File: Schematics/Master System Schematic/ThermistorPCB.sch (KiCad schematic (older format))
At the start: 0 parts

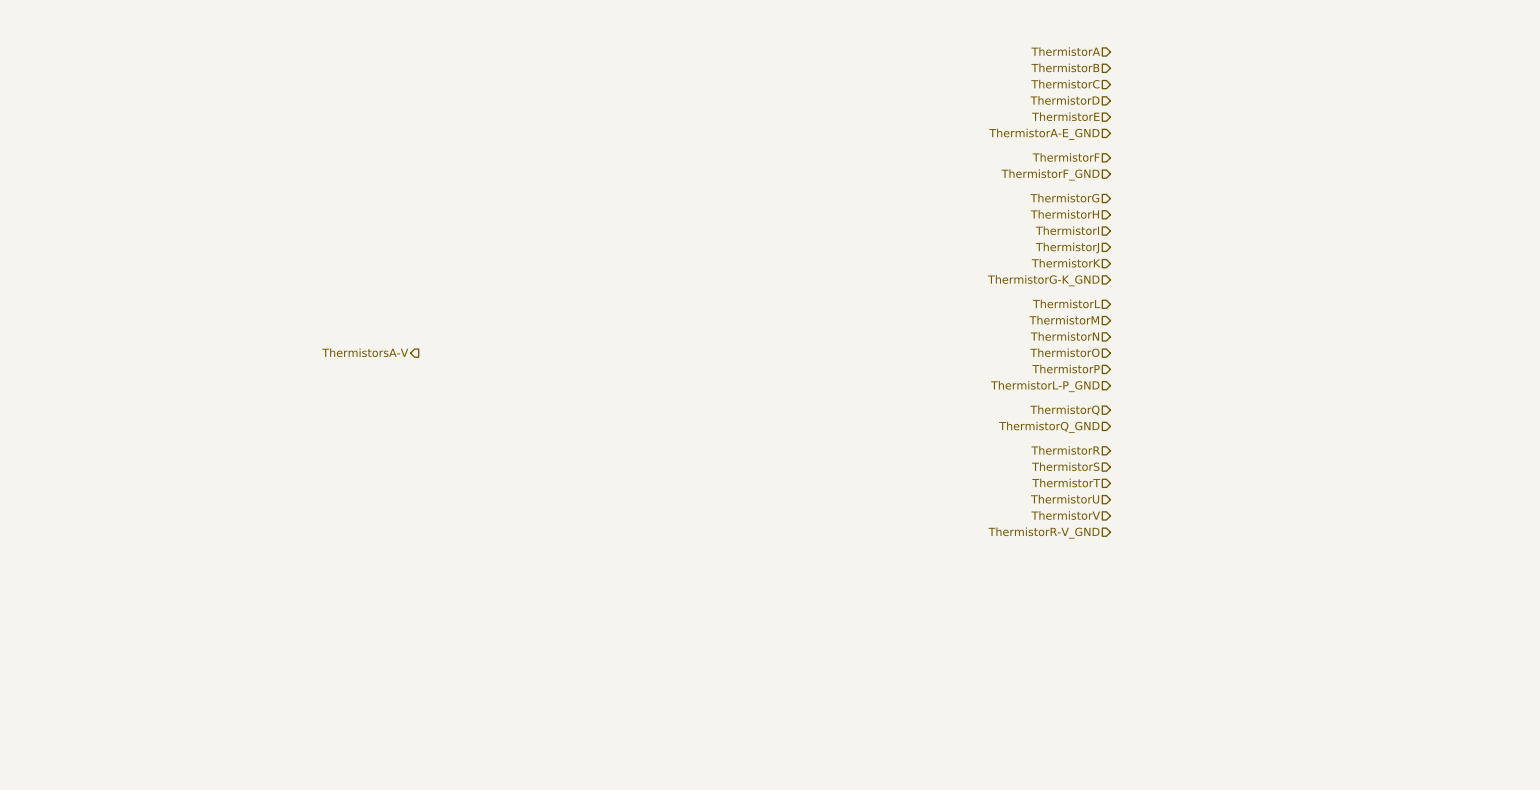
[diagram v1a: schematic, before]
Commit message: added thermistor expansion to Accumulator container
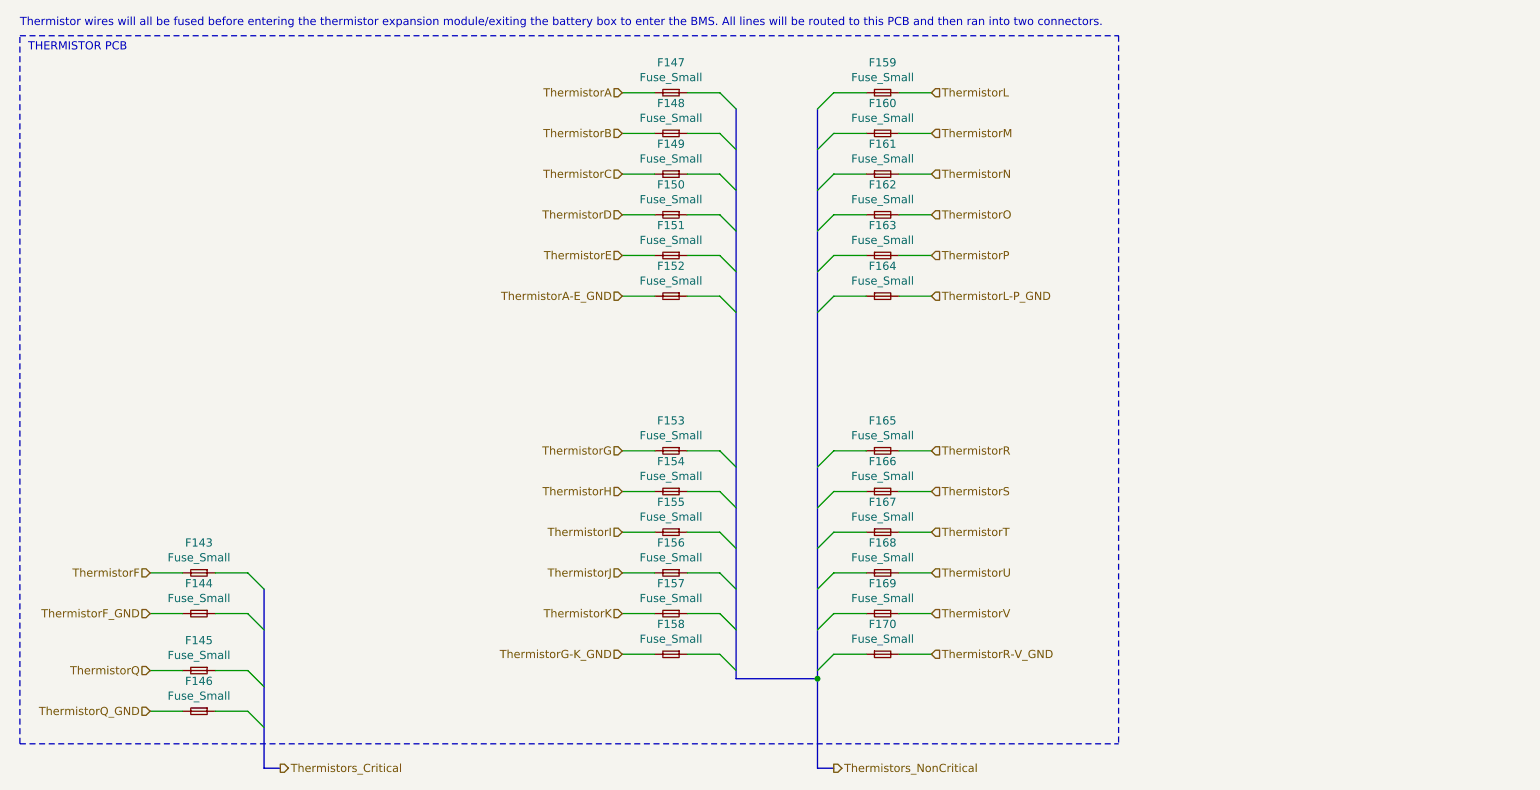
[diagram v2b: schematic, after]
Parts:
- added F143, F144, F145, F146, F147, F148, F149, F150, F151, F152, F153, F154, F155, F156, F157, F158, F159, F160, F161, F162, F163, F164, F165, F166, F167, F168, F169, F170: Fuse_Small, symbol Device:Fuse_Small
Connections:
- net ThermistorA: now also F147.2
- net ThermistorA-E_GND: now also F152.2
- net ThermistorB: now also F148.2
- net ThermistorC: now also F149.2
- net ThermistorD: now also F150.2
- net ThermistorE: now also F151.2
- net ThermistorF: now also F143.2
- net ThermistorF_GND: now also F144.2
- net ThermistorG: now also F153.2
- net ThermistorG-K_GND: now also F158.2
- net ThermistorH: now also F154.2
- net ThermistorI: now also F155.2
- net ThermistorJ: now also F156.2
- net ThermistorK: now also F157.2
- net ThermistorL: now also F159.2
- net ThermistorL-P_GND: now also F164.2
- net ThermistorM: now also F160.2
- net ThermistorN: now also F161.2
- net ThermistorO: now also F162.2
- net ThermistorP: now also F163.2
- net ThermistorQ: now also F145.2
- net ThermistorQ_GND: now also F146.2
- net ThermistorR: now also F165.2
- net ThermistorR-V_GND: now also F170.2
- net ThermistorS: now also F166.2
- net ThermistorT: now also F167.2
- net ThermistorU: now also F168.2
- net ThermistorV: now also F169.2
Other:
- note added: "THERMISTOR PCB"
- note added: "Thermistor wires will all be fused before entering the thermistor expansion module/exiting the battery box to enter the BMS. All lines will be routed to this PCB and then ran into two connectors."

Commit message: fixed therm boards
fixed therm board implementation
beginning accumulator redraw
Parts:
- removed F153, F154, F155, F156, F157, F158, F159, F160, F161, F162, F163, F164, F165, F166, F167, F168, F169, F170: Fuse_Small, symbol Device:Fuse_Small
- added F? (x18): Fuse_Small, symbol Device:Fuse_Small
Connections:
- net ThermistorG: now also F?.2
- net ThermistorH: now also F?.2
- net ThermistorI: now also F?.2
- net ThermistorJ: now also F?.2
- net ThermistorK: now also F?.2
- net ThermistorL: now also F?.2
- net ThermistorM: now also F?.2
- net ThermistorN: now also F?.2
- net ThermistorO: now also F?.2
- net ThermistorP: now also F?.2
- net ThermistorR: now also F?.2
- net ThermistorS: now also F?.2
- net ThermistorT: now also F?.2
- net ThermistorU: now also F?.2
- net ThermistorV: now also F?.2
- net ThermistorA-E_GND renamed ThermistorA_GND
- new net ThermistorG_GND: F?.2
- new net ThermistorL_GND: F?.2
- new net ThermistorR_GND: F?.2
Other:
- moved on the sheet: F143, F144, F145, F146, F147, F148, F149, F150, F151, F152

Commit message: roughly spread out accumulator components, updated therms boards
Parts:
- gave numbers to parts that had none: 18

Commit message: Finished master and accum cleanup
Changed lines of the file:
@@
 $Descr A 11000 8500
 encoding utf-8
-Sheet 17 22
+Sheet 11 22
 Title "Sgment Thermistor PCB"
 Date "2020-11-11"
@@
 AR Path="/5F45B05E/602D10EE/5FDCE36A" Ref="F137"  Part="1"
 AR Path="/5F45B05E/6031BDF8/5FDCE36A" Ref="F165"  Part="1"
-F 0 "F165" H 3000 3385 50  0000 C CNN
+F 0 "F179" H 3000 3385 50  0000 C CNN
 F 1 "Fuse_Small" H 3000 3294 50  0000 C CNN
 F 2 "" H 3000 3200 50  0001 C CNN
@@
 AR Path="/5F45B05E/602D10EE/5FDCE957" Ref="F138"  Part="1"
 AR Path="/5F45B05E/6031BDF8/5FDCE957" Ref="F166"  Part="1"
-F 0 "F166" H 3000 3685 50  0000 C CNN
+F 0 "F180" H 3000 3685 50  0000 C CNN
 F 1 "Fuse_Small" H 3000 3594 50  0000 C CNN
 F 2 "" H 3000 3500 50  0001 C CNN
@@
 AR Path="/5F45B05E/602D10EE/5FDD20B1" Ref="F139"  Part="1"
 AR Path="/5F45B05E/6031BDF8/5FDD20B1" Ref="F167"  Part="1"
-F 0 "F167" H 3000 4735 50  0000 C CNN
+F 0 "F171" H 3000 4735 50  0000 C CNN
 F 1 "Fuse_Small" H 3000 4644 50  0000 C CNN
 F 2 "" H 3000 4550 50  0001 C CNN
@@
 AR Path="/5F45B05E/602D10EE/5FDD20B7" Ref="F140"  Part="1"
 AR Path="/5F45B05E/6031BDF8/5FDD20B7" Ref="F168"  Part="1"
-F 0 "F168" H 3000 4985 50  0000 C CNN
+F 0 "F172" H 3000 4985 50  0000 C CNN
 F 1 "Fuse_Small" H 3000 4894 50  0000 C CNN
 F 2 "" H 3000 4800 50  0001 C CNN
@@
 AR Path="/5F45B05E/602D10EE/5FDD283F" Ref="F153"  Part="1"
 AR Path="/5F45B05E/6031BDF8/5FDD283F" Ref="F191"  Part="1"
-F 0 "F191" H 6850 4735 50  0000 C CNN
+F 0 "F173" H 6850 4735 50  0000 C CNN
 F 1 "Fuse_Small" H 6850 4644 50  0000 C CNN
 F 2 "" H 6850 4550 50  0001 C CNN
@@
 AR Path="/5F45B05E/602D10EE/5FDD2845" Ref="F154"  Part="1"
 AR Path="/5F45B05E/6031BDF8/5FDD2845" Ref="F192"  Part="1"
-F 0 "F192" H 6850 4985 50  0000 C CNN
+F 0 "F174" H 6850 4985 50  0000 C CNN
 F 1 "Fuse_Small" H 6850 4894 50  0000 C CNN
 F 2 "" H 6850 4800 50  0001 C CNN
@@
 AR Path="/5F45B05E/602D10EE/5FDCCCB1" Ref="F133"  Part="1"
 AR Path="/5F45B05E/6031BDF8/5FDCCCB1" Ref="F161"  Part="1"
-F 0 "F161" H 3000 2185 50  0000 C CNN
+F 0 "F175" H 3000 2185 50  0000 C CNN
 F 1 "Fuse_Small" H 3000 2094 50  0000 C CNN
 F 2 "" H 3000 2000 50  0001 C CNN
@@
 AR Path="/5F45B05E/602D10EE/5FDCD1AF" Ref="F134"  Part="1"
 AR Path="/5F45B05E/6031BDF8/5FDCD1AF" Ref="F162"  Part="1"
-F 0 "F162" H 3000 2485 50  0000 C CNN
+F 0 "F176" H 3000 2485 50  0000 C CNN
 F 1 "Fuse_Small" H 3000 2394 50  0000 C CNN
 F 2 "" H 3000 2300 50  0001 C CNN
@@
 AR Path="/5F45B05E/602D10EE/5FDCD7E4" Ref="F135"  Part="1"
 AR Path="/5F45B05E/6031BDF8/5FDCD7E4" Ref="F163"  Part="1"
-F 0 "F163" H 3000 2785 50  0000 C CNN
+F 0 "F177" H 3000 2785 50  0000 C CNN
 F 1 "Fuse_Small" H 3000 2694 50  0000 C CNN
 F 2 "" H 3000 2600 50  0001 C CNN
@@
 AR Path="/5F45B05E/602D10EE/5FDCDD70" Ref="F136"  Part="1"
 AR Path="/5F45B05E/6031BDF8/5FDCDD70" Ref="F164"  Part="1"
-F 0 "F164" H 3000 3085 50  0000 C CNN
+F 0 "F178" H 3000 3085 50  0000 C CNN
 F 1 "Fuse_Small" H 3000 2994 50  0000 C CNN
 F 2 "" H 3000 2900 50  0001 C CNN
@@
 AR Path="/5F45B05E/602D10EE/5FCBC472" Ref="F145"  Part="1"
 AR Path="/5F45B05E/6031BDF8/5FCBC472" Ref="F183"  Part="1"
-F 0 "F183" H 4400 3385 50  0000 C CNN
+F 0 "F91" H 4400 3385 50  0000 C CNN
 F 1 "Fuse_Small" H 4400 3294 50  0000 C CNN
 F 2 "" H 4400 3200 50  0001 C CNN
@@
 AR Path="/5F45B05E/602D10EE/5FCBC478" Ref="F146"  Part="1"
 AR Path="/5F45B05E/6031BDF8/5FCBC478" Ref="F184"  Part="1"
-F 0 "F184" H 4400 3685 50  0000 C CNN
+F 0 "F92" H 4400 3685 50  0000 C CNN
 F 1 "Fuse_Small" H 4400 3594 50  0000 C CNN
 F 2 "" H 4400 3500 50  0001 C CNN
@@
 AR Path="/5F45B05E/602D10EE/5FCBC47E" Ref="F141"  Part="1"
 AR Path="/5F45B05E/6031BDF8/5FCBC47E" Ref="F169"  Part="1"
-F 0 "F169" H 4400 2185 50  0000 C CNN
+F 0 "F87" H 4400 2185 50  0000 C CNN
 F 1 "Fuse_Small" H 4400 2094 50  0000 C CNN
 F 2 "" H 4400 2000 50  0001 C CNN
@@
 AR Path="/5F45B05E/602D10EE/5FCBC484" Ref="F142"  Part="1"
 AR Path="/5F45B05E/6031BDF8/5FCBC484" Ref="F170"  Part="1"
-F 0 "F170" H 4400 2485 50  0000 C CNN
+F 0 "F88" H 4400 2485 50  0000 C CNN
 F 1 "Fuse_Small" H 4400 2394 50  0000 C CNN
 F 2 "" H 4400 2300 50  0001 C CNN
@@
 AR Path="/5F45B05E/602D10EE/5FCBC48A" Ref="F143"  Part="1"
 AR Path="/5F45B05E/6031BDF8/5FCBC48A" Ref="F181"  Part="1"
-F 0 "F181" H 4400 2785 50  0000 C CNN
+F 0 "F89" H 4400 2785 50  0000 C CNN
 F 1 "Fuse_Small" H 4400 2694 50  0000 C CNN
 F 2 "" H 4400 2600 50  0001 C CNN
@@
 AR Path="/5F45B05E/602D10EE/5FCBC490" Ref="F144"  Part="1"
 AR Path="/5F45B05E/6031BDF8/5FCBC490" Ref="F182"  Part="1"
-F 0 "F182" H 4400 3085 50  0000 C CNN
+F 0 "F90" H 4400 3085 50  0000 C CNN
 F 1 "Fuse_Small" H 4400 2994 50  0000 C CNN
 F 2 "" H 4400 2900 50  0001 C CNN
@@
 AR Path="/5F45B05E/602D10EE/5FCC48E6" Ref="F151"  Part="1"
 AR Path="/5F45B05E/6031BDF8/5FCC48E6" Ref="F189"  Part="1"
-F 0 "F189" H 6850 3385 50  0000 C CNN
+F 0 "F97" H 6850 3385 50  0000 C CNN
 F 1 "Fuse_Small" H 6850 3294 50  0000 C CNN
 F 2 "" H 6850 3200 50  0001 C CNN
@@
 AR Path="/5F45B05E/602D10EE/5FCC48EC" Ref="F152"  Part="1"
 AR Path="/5F45B05E/6031BDF8/5FCC48EC" Ref="F190"  Part="1"
-F 0 "F190" H 6850 3685 50  0000 C CNN
+F 0 "F98" H 6850 3685 50  0000 C CNN
 F 1 "Fuse_Small" H 6850 3594 50  0000 C CNN
 F 2 "" H 6850 3500 50  0001 C CNN
@@
 AR Path="/5F45B05E/602D10EE/5FCC48F2" Ref="F147"  Part="1"
 AR Path="/5F45B05E/6031BDF8/5FCC48F2" Ref="F185"  Part="1"
-F 0 "F185" H 6850 2185 50  0000 C CNN
+F 0 "F93" H 6850 2185 50  0000 C CNN
 F 1 "Fuse_Small" H 6850 2094 50  0000 C CNN
 F 2 "" H 6850 2000 50  0001 C CNN
@@
 AR Path="/5F45B05E/602D10EE/5FCC48F8" Ref="F148"  Part="1"
 AR Path="/5F45B05E/6031BDF8/5FCC48F8" Ref="F186"  Part="1"
-F 0 "F186" H 6850 2485 50  0000 C CNN
+F 0 "F94" H 6850 2485 50  0000 C CNN
 F 1 "Fuse_Small" H 6850 2394 50  0000 C CNN
 F 2 "" H 6850 2300 50  0001 C CNN
@@
 AR Path="/5F45B05E/602D10EE/5FCC48FE" Ref="F149"  Part="1"
 AR Path="/5F45B05E/6031BDF8/5FCC48FE" Ref="F187"  Part="1"
-F 0 "F187" H 6850 2785 50  0000 C CNN
+F 0 "F95" H 6850 2785 50  0000 C CNN
 F 1 "Fuse_Small" H 6850 2694 50  0000 C CNN
 F 2 "" H 6850 2600 50  0001 C CNN
@@
 AR Path="/5F45B05E/602D10EE/5FCC4904" Ref="F150"  Part="1"
 AR Path="/5F45B05E/6031BDF8/5FCC4904" Ref="F188"  Part="1"
-F 0 "F188" H 6850 3085 50  0000 C CNN
+F 0 "F96" H 6850 3085 50  0000 C CNN
 F 1 "Fuse_Small" H 6850 2994 50  0000 C CNN
 F 2 "" H 6850 2900 50  0001 C CNN
@@
 AR Path="/5F45B05E/602D10EE/5FCC492A" Ref="F159"  Part="1"
 AR Path="/5F45B05E/6031BDF8/5FCC492A" Ref="F197"  Part="1"
-F 0 "F197" H 8250 3385 50  0000 C CNN
+F 0 "F103" H 8250 3385 50  0000 C CNN
 F 1 "Fuse_Small" H 8250 3294 50  0000 C CNN
 F 2 "" H 8250 3200 50  0001 C CNN
@@
 AR Path="/5F45B05E/602D10EE/5FCC4930" Ref="F160"  Part="1"
 AR Path="/5F45B05E/6031BDF8/5FCC4930" Ref="F198"  Part="1"
-F 0 "F198" H 8250 3685 50  0000 C CNN
+F 0 "F104" H 8250 3685 50  0000 C CNN
 F 1 "Fuse_Small" H 8250 3594 50  0000 C CNN
 F 2 "" H 8250 3500 50  0001 C CNN
@@
 AR Path="/5F45B05E/602D10EE/5FCC4936" Ref="F155"  Part="1"
 AR Path="/5F45B05E/6031BDF8/5FCC4936" Ref="F193"  Part="1"
-F 0 "F193" H 8250 2185 50  0000 C CNN
+F 0 "F99" H 8250 2185 50  0000 C CNN
 F 1 "Fuse_Small" H 8250 2094 50  0000 C CNN
 F 2 "" H 8250 2000 50  0001 C CNN
@@
 AR Path="/5F45B05E/602D10EE/5FCC493C" Ref="F156"  Part="1"
 AR Path="/5F45B05E/6031BDF8/5FCC493C" Ref="F194"  Part="1"
-F 0 "F194" H 8250 2485 50  0000 C CNN
+F 0 "F100" H 8250 2485 50  0000 C CNN
 F 1 "Fuse_Small" H 8250 2394 50  0000 C CNN
 F 2 "" H 8250 2300 50  0001 C CNN
@@
 AR Path="/5F45B05E/602D10EE/5FCC4942" Ref="F157"  Part="1"
 AR Path="/5F45B05E/6031BDF8/5FCC4942" Ref="F195"  Part="1"
-F 0 "F195" H 8250 2785 50  0000 C CNN
+F 0 "F101" H 8250 2785 50  0000 C CNN
 F 1 "Fuse_Small" H 8250 2694 50  0000 C CNN
 F 2 "" H 8250 2600 50  0001 C CNN
@@
 AR Path="/5F45B05E/602D10EE/5FCC4948" Ref="F158"  Part="1"
 AR Path="/5F45B05E/6031BDF8/5FCC4948" Ref="F196"  Part="1"
-F 0 "F196" H 8250 3085 50  0000 C CNN
+F 0 "F102" H 8250 3085 50  0000 C CNN
 F 1 "Fuse_Small" H 8250 2994 50  0000 C CNN
 F 2 "" H 8250 2900 50  0001 C CNN
